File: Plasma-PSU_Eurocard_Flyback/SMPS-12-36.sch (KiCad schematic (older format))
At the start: 41 parts

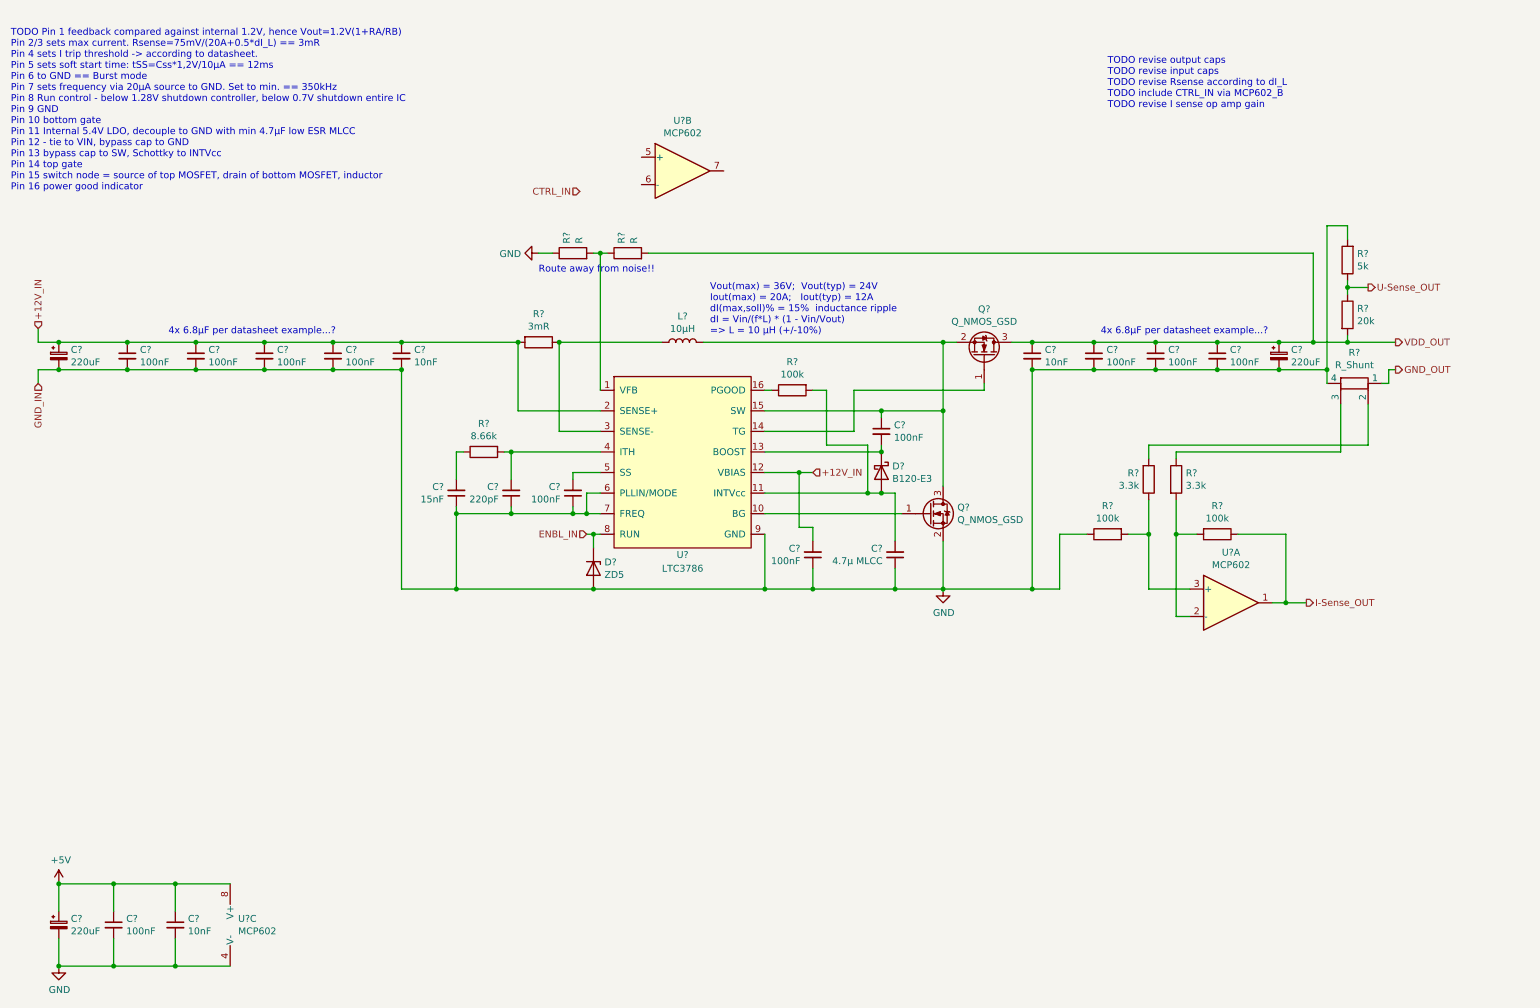
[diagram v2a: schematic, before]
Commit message: Filter caps & Rsense revised
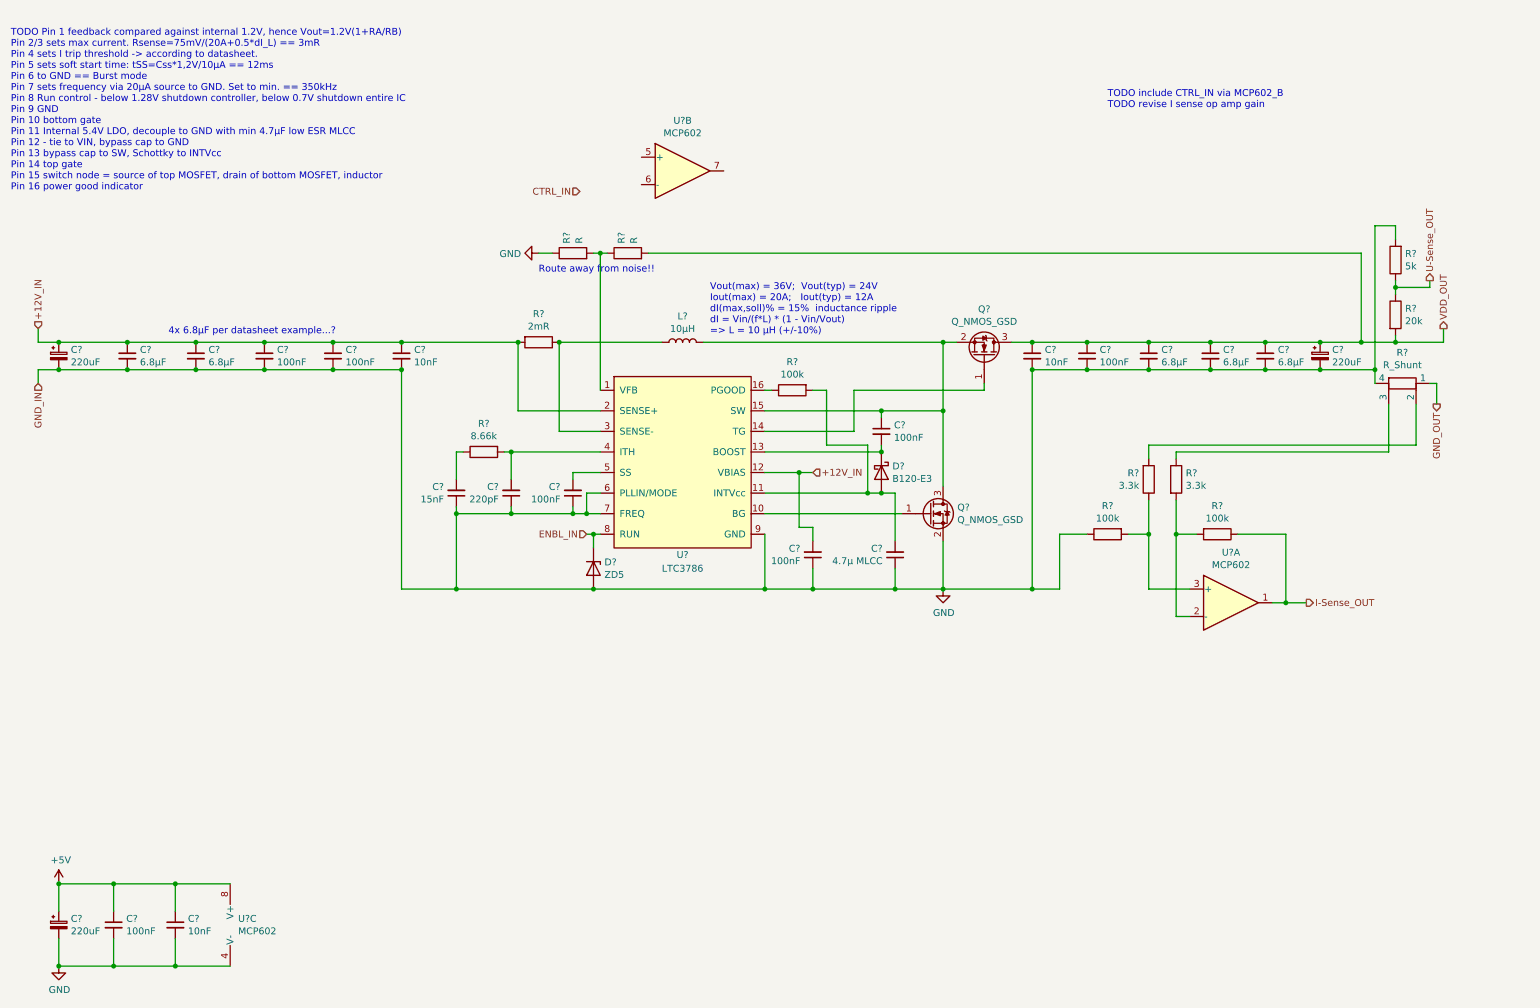
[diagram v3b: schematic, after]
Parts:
- added C?: 6.8µF, symbol Device:C_Small
- C? (x4): value 100nF -> 6.8µF
- R?: value 3mR -> 2mR
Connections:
- net GND: now also C?.2
- net VDD_OUT: now also C?.1
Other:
- note added: "TODO include CTRL_IN via MCP602_B\nTODO revise I sense op amp gain"
- note removed: "TODO revise output caps\nTODO revise input caps\nTODO revise Rsense according to dI_L\nTODO include CTRL_IN via MCP602_B\nTODO revise I sense op amp gain"
- moved on the sheet: C?, R?
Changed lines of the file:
@@
 Text HLabel 850  3250 3    50   Input ~ 0
 GND_IN
-Text HLabel 10750 2950 2    50   Output ~ 0
+Text HLabel 11100 2850 1    50   Output ~ 0
 VDD_OUT
-Text HLabel 10750 3150 2    50   Output ~ 0
+Text HLabel 11050 3400 3    50   Output ~ 0
 GND_OUT
 Text HLabel 4800 1850 0    50   Input ~ 0
@@
 Text HLabel 10100 4850 2    50   Output ~ 0
 I-Sense_OUT
-Text HLabel 10550 2550 2    50   Output ~ 0
+Text HLabel 11000 2500 1    50   Output ~ 0
 U-Sense_OUT
 $Comp
@@
 P 1500 3050
 F 0 "C?" H 1592 3096 50  0000 L CNN
-F 1 "100nF" H 1592 3005 50  0000 L CNN
+F 1 "6.8µF" H 1592 3005 50  0000 L CNN
 F 2 "" H 1500 3050 50  0001 C CNN
 F 3 "~" H 1500 3050 50  0001 C CNN
@@
 P 2000 3050
 F 0 "C?" H 2092 3096 50  0000 L CNN
-F 1 "100nF" H 2092 3005 50  0000 L CNN
+F 1 "6.8µF" H 2092 3005 50  0000 L CNN
 F 2 "" H 2000 3050 50  0001 C CNN
 F 3 "~" H 2000 3050 50  0001 C CNN
@@
 L Device:C_Small C?
 U 1 1 5E8B8979
-P 9450 3050
-F 0 "C?" H 9542 3096 50  0000 L CNN
-F 1 "100nF" H 9542 3005 50  0000 L CNN
-F 2 "" H 9450 3050 50  0001 C CNN
-F 3 "~" H 9450 3050 50  0001 C CNN
-	1    9450 3050
+P 9400 3050
+F 0 "C?" H 9492 3096 50  0000 L CNN
+F 1 "6.8µF" H 9492 3005 50  0000 L CNN
+F 2 "" H 9400 3050 50  0001 C CNN
+F 3 "~" H 9400 3050 50  0001 C CNN
+	1    9400 3050
 	1    0    0    -1
 $EndComp
@@
 L Device:R R?
 U 1 1 5E8C18D8
-P 10400 2350
-F 0 "R?" H 10330 2304 50  0000 R CNN
-F 1 "5k" H 10330 2395 50  0000 R CNN
-F 2 "" V 10330 2350 50  0001 C CNN
-F 3 "~" H 10400 2350 50  0001 C CNN
-	1    10400 2350
+P 10750 2350
+F 0 "R?" H 10680 2304 50  0000 R CNN
+F 1 "5k" H 10680 2395 50  0000 R CNN
+F 2 "" V 10680 2350 50  0001 C CNN
+F 3 "~" H 10750 2350 50  0001 C CNN
+	1    10750 2350
 	-1   0    0    1
 $EndComp
@@
 L Device:R R?
 U 1 1 5E8C1FE2
-P 10400 2750
-F 0 "R?" H 10470 2796 50  0000 L CNN
-F 1 "20k" H 10470 2705 50  0000 L CNN
-F 2 "" V 10330 2750 50  0001 C CNN
-F 3 "~" H 10400 2750 50  0001 C CNN
-	1    10400 2750
+P 10750 2750
+F 0 "R?" H 10820 2796 50  0000 L CNN
+F 1 "20k" H 10820 2705 50  0000 L CNN
+F 2 "" V 10680 2750 50  0001 C CNN
+F 3 "~" H 10750 2750 50  0001 C CNN
+	1    10750 2750
 	1    0    0    -1
 $EndComp
@@
 L Device:R_Shunt R?
 U 1 1 5E8C5243
-P 10450 3250
-F 0 "R?" V 10225 3250 50  0000 C CNN
-F 1 "R_Shunt" V 10316 3250 50  0000 C CNN
-F 2 "" V 10380 3250 50  0001 C CNN
-F 3 "~" H 10450 3250 50  0001 C CNN
-	1    10450 3250
+P 10800 3250
+F 0 "R?" V 10575 3250 50  0000 C CNN
+F 1 "R_Shunt" V 10666 3250 50  0000 C CNN
+F 2 "" V 10730 3250 50  0001 C CNN
+F 3 "~" H 10800 3250 50  0001 C CNN
+	1    10800 3250
 	0    1    1    0
 $EndComp
@@
 Connection ~ 9950 4850
 Wire Wire Line
-	10400 2500 10400 2550
-Wire Wire Line
-	10550 2550 10400 2550
-Connection ~ 10400 2550
-Wire Wire Line
-	10400 2550 10400 2600
+	10750 2500 10750 2550
+Connection ~ 10750 2550
+Wire Wire Line
+	10750 2550 10750 2600
 Wire Wire Line
 	9950 4850 10100 4850
@@
 P 4500 2950
 F 0 "R?" V 4293 2950 50  0000 C CNN
-F 1 "3mR" V 4384 2950 50  0000 C CNN
+F 1 "2mR" V 4384 2950 50  0000 C CNN
 F 2 "" V 4430 2950 50  0001 C CNN
 F 3 "~" H 4500 2950 50  0001 C CNN
@@
 	4500 2300 4600 2300
 Wire Wire Line
-	10150 2950 10150 2300
+	10500 2950 10500 2300
 $Comp
 L Device:C_Small C?
@@
 Connection ~ 6150 4750
 Text Notes 8650 1250 0    50   ~ 0
-TODO revise output caps\nTODO revise input caps\nTODO revise Rsense according to dI_L\nTODO include CTRL_IN via MCP602_B\nTODO revise I sense op amp gain
+TODO include CTRL_IN via MCP602_B\nTODO revise I sense op amp gain
 $Comp
 L Device:D_Zener D?
@@
 L Device:C_Small C?
 U 1 1 5EB20DC9
-P 9000 3050
-F 0 "C?" H 9092 3096 50  0000 L CNN
-F 1 "100nF" H 9092 3005 50  0000 L CNN
-F 2 "" H 9000 3050 50  0001 C CNN
-F 3 "~" H 9000 3050 50  0001 C CNN
-	1    9000 3050
-	1    0    0    -1
-$EndComp
-Wire Wire Line
-	7950 2950 8100 2950
-Wire Wire Line
-	9150 3750 10350 3750
-Wire Wire Line
-	5300 2300 10150 2300
-Connection ~ 9900 2950
-Connection ~ 9450 2950
-Wire Wire Line
-	9450 2950 9900 2950
-Connection ~ 9450 3150
-Wire Wire Line
-	9450 3150 9900 3150
-Connection ~ 9000 2950
-Connection ~ 9000 3150
+P 8950 3050
+F 0 "C?" H 9042 3096 50  0000 L CNN
+F 1 "6.8µF" H 9042 3005 50  0000 L CNN
+F 2 "" H 8950 3050 50  0001 C CNN
+F 3 "~" H 8950 3050 50  0001 C CNN
+	1    8950 3050
+	1    0    0    -1
+$EndComp
 $Comp
 L Device:C_Small C?
 U 1 1 5EB34187
-P 8550 3050
-F 0 "C?" H 8642 3096 50  0000 L CNN
-F 1 "100nF" H 8642 3005 50  0000 L CNN
-F 2 "" H 8550 3050 50  0001 C CNN
-F 3 "~" H 8550 3050 50  0001 C CNN
-	1    8550 3050
-	1    0    0    -1
-$EndComp
-Connection ~ 8550 2950
-Connection ~ 8550 3150
+P 8500 3050
+F 0 "C?" H 8592 3096 50  0000 L CNN
+F 1 "100nF" H 8592 3005 50  0000 L CNN
+F 2 "" H 8500 3050 50  0001 C CNN
+F 3 "~" H 8500 3050 50  0001 C CNN
+	1    8500 3050
+	1    0    0    -1
+$EndComp
 $Comp
 L Device:CP_Small C?
 U 1 1 5EB34616
-P 9900 3050
-F 0 "C?" H 9988 3096 50  0000 L CNN
-F 1 "220uF" H 9988 3005 50  0000 L CNN
-F 2 "" H 9900 3050 50  0001 C CNN
-F 3 "~" H 9900 3050 50  0001 C CNN
-	1    9900 3050
+P 10200 3050
+F 0 "C?" H 10288 3096 50  0000 L CNN
+F 1 "220uF" H 10288 3005 50  0000 L CNN
+F 2 "" H 10200 3050 50  0001 C CNN
+F 3 "~" H 10200 3050 50  0001 C CNN
+	1    10200 3050
 	1    0    0    -1
 $EndComp
@@
 Wire Wire Line
 	7450 4750 8100 4750
-Wire Wire Line
-	8100 3150 8550 3150
-Wire Wire Line
-	8100 2950 8550 2950
-Wire Wire Line
-	8550 2950 9000 2950
-Wire Wire Line
-	8550 3150 9000 3150
-Wire Wire Line
-	9000 3150 9450 3150
-Wire Wire Line
-	9000 2950 9450 2950
 Text Notes 5750 2900 0    50   ~ 0
 Vout(max) = 36V;  Vout(typ) = 24V\nIout(max) = 20A;   Iout(typ) = 12A\ndI(max,soll)% = 15%  inductance ripple\ndI = Vin/(f*L) * (1 - Vin/Vout)\n=> L = 10 µH (+/-10%)
@@
 Wire Wire Line
 	7750 3300 7750 3250
-Text Notes 8600 2900 0    50   ~ 0
-4x 6.8µF per datasheet example...?
 Text Notes 1800 2900 0    50   ~ 0
 4x 6.8µF per datasheet example...?
@@
 Connection ~ 1000 6900
 Wire Wire Line
-	10650 3250 10700 3250
-Wire Wire Line
-	10700 3250 10700 3150
-Wire Wire Line
-	10700 3150 10750 3150
-Connection ~ 9900 3150
-Wire Wire Line
-	9900 2950 10150 2950
-Wire Wire Line
-	10550 3700 10550 3400
-Wire Wire Line
-	8950 3700 10550 3700
-Wire Wire Line
-	10350 3400 10350 3750
-Wire Wire Line
-	9900 3150 10250 3150
-Wire Wire Line
-	10250 3150 10250 3250
-Connection ~ 10150 2950
-Wire Wire Line
-	10150 2950 10400 2950
-Wire Wire Line
-	10400 2950 10400 2900
-Connection ~ 10400 2950
-Wire Wire Line
-	10400 2950 10750 2950
-Wire Wire Line
-	10400 2200 10400 2100
-Wire Wire Line
-	10400 2100 10250 2100
-Wire Wire Line
-	10250 2100 10250 3150
-Connection ~ 10250 3150
+	11000 3250 11050 3250
+Wire Wire Line
+	10900 3700 10900 3400
+Wire Wire Line
+	10700 3400 10700 3750
+Wire Wire Line
+	10600 3150 10600 3250
+Connection ~ 10500 2950
+Wire Wire Line
+	10500 2950 10750 2950
+Wire Wire Line
+	10750 2950 10750 2900
+Connection ~ 10750 2950
+Wire Wire Line
+	10750 2950 11100 2950
+Wire Wire Line
+	10750 2200 10750 2100
+Wire Wire Line
+	10750 2100 10600 2100
+Wire Wire Line
+	10600 2100 10600 3150
+Connection ~ 10600 3150
+Wire Wire Line
+	11050 3400 11050 3250
+Wire Wire Line
+	11000 2550 11000 2500
+Wire Wire Line
+	10750 2550 11000 2550
+Wire Wire Line
+	11100 2950 11100 2850
+$Comp
+L Device:C_Small C?
+U 1 1 5E8DF31F
+P 9800 3050
+F 0 "C?" H 9892 3096 50  0000 L CNN
+F 1 "6.8µF" H 9892 3005 50  0000 L CNN
+F 2 "" H 9800 3050 50  0001 C CNN
+F 3 "~" H 9800 3050 50  0001 C CNN
+	1    9800 3050
+	1    0    0    -1
+$EndComp
+Connection ~ 9400 2950
+Connection ~ 9400 3150
+Connection ~ 9800 2950
+Connection ~ 9800 3150
+Connection ~ 8950 2950
+Connection ~ 8950 3150
+Connection ~ 8500 2950
+Connection ~ 8500 3150
+Wire Wire Line
+	7950 2950 8100 2950
+Wire Wire Line
+	9400 2950 9800 2950
+Wire Wire Line
+	9400 3150 9800 3150
+Wire Wire Line
+	8100 3150 8500 3150
+Wire Wire Line
+	8100 2950 8500 2950
+Wire Wire Line
+	8950 3150 9400 3150
+Wire Wire Line
+	8950 2950 9400 2950
+Wire Wire Line
+	8500 2950 8950 2950
+Wire Wire Line
+	8500 3150 8950 3150
+Wire Wire Line
+	9800 2950 10200 2950
+Connection ~ 10200 2950
+Wire Wire Line
+	10200 2950 10500 2950
+Wire Wire Line
+	9800 3150 10200 3150
+Connection ~ 10200 3150
+Wire Wire Line
+	10200 3150 10600 3150
+Wire Wire Line
+	5300 2300 10500 2300
+Wire Wire Line
+	8950 3700 10900 3700
+Wire Wire Line
+	9150 3750 10700 3750
 $EndSCHEMATC

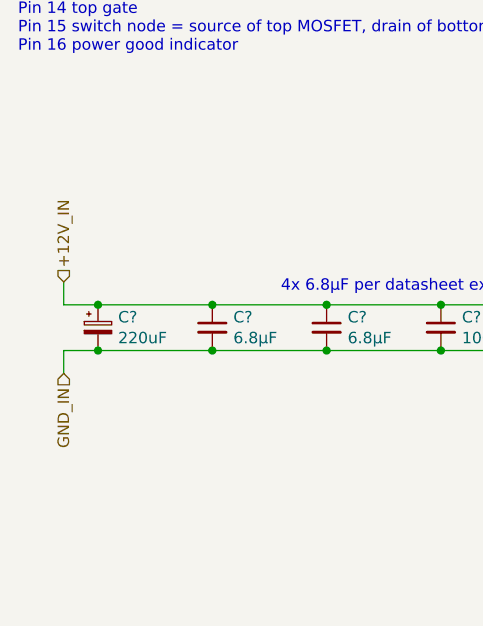
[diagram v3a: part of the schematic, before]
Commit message: Block diagram, Connectivity, Isolation
- First page reservered for block diagram
- Connectors moved to separate sheet
- Opto-isolators for signal inputs on HV board
- Fuse added to SMPS
- Pinheader for Arduino pin-out, UART, I2C, SPI
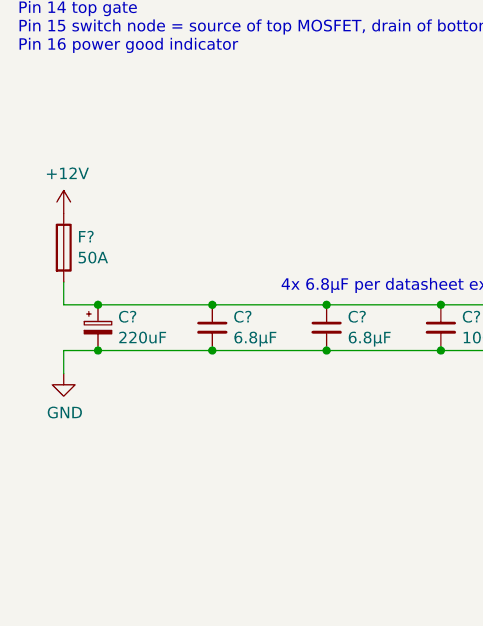
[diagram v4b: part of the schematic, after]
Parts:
- added F?: 50A, symbol Device:Fuse
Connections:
- net +12V_IN: no longer C?.1, C?.1, C?.1, C?.1, C?.1, C?.1, R?.2, U?.2 (SENSE+)
- new net: C?.1, C?.1, C?.1, C?.1, C?.1, C?.1, F?.2, R?.2, U?.2 (SENSE+)
- new net +12V: F?.1
